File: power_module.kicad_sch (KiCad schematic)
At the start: 42 parts, among them IC1 LT8609AEDDM#PBF, IC2 LM2678SX-ADJ/NOPB, IC3 LM2678SX-ADJ/NOPB, IC4 LM2678SX-ADJ/NOPB, J1 Conn_01x02_Pin

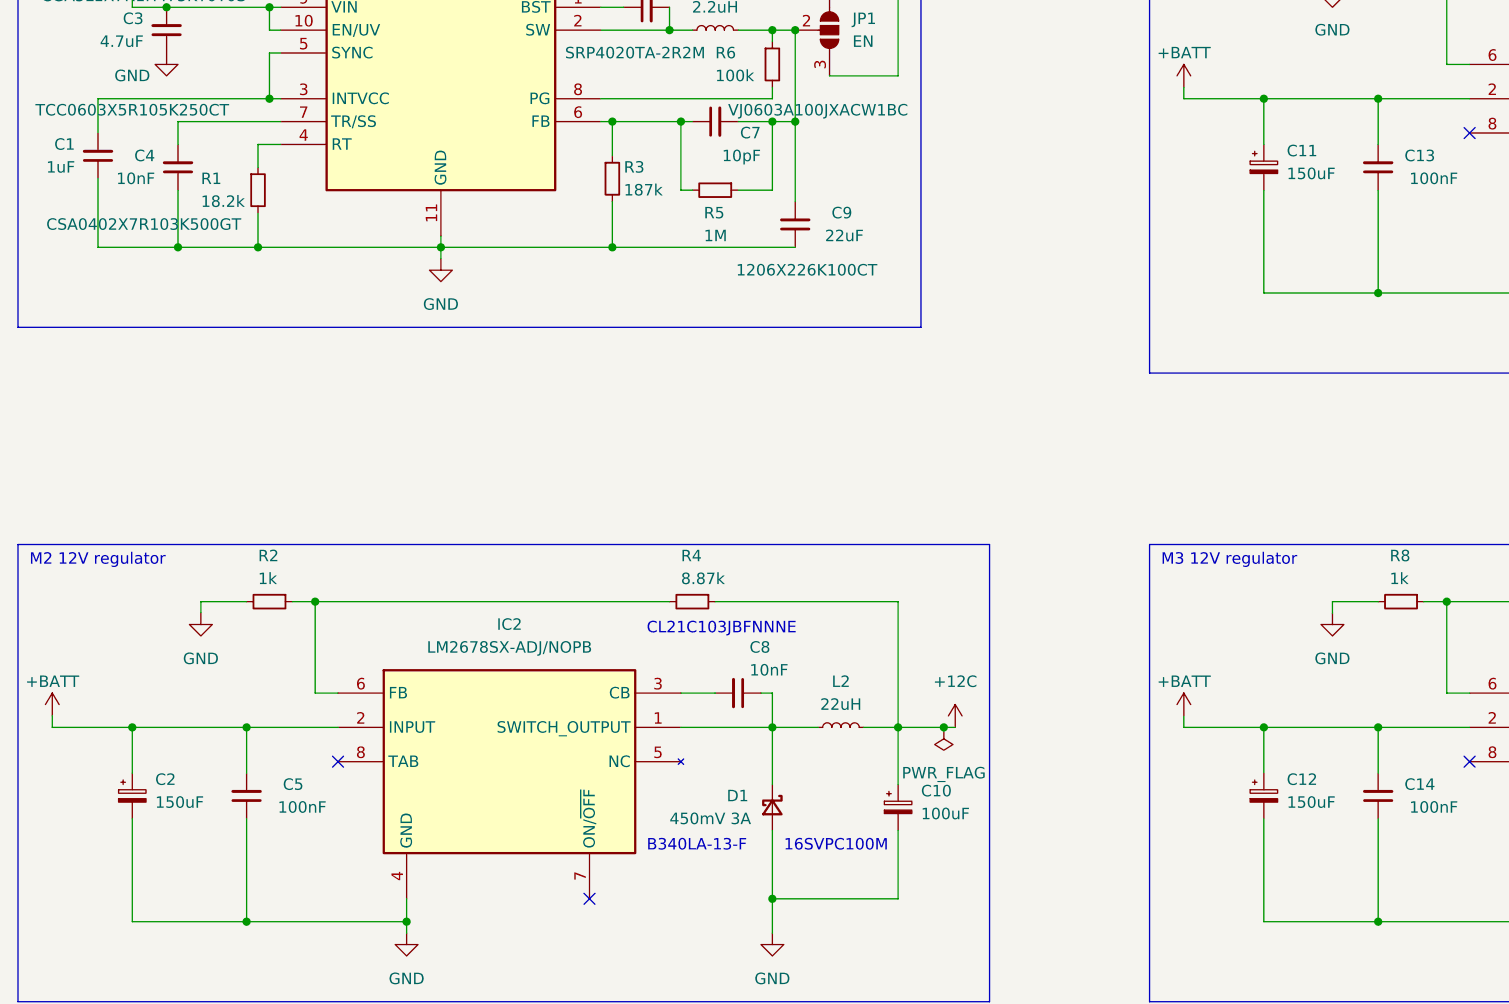
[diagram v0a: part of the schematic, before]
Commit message: completed 12 V regulators routing
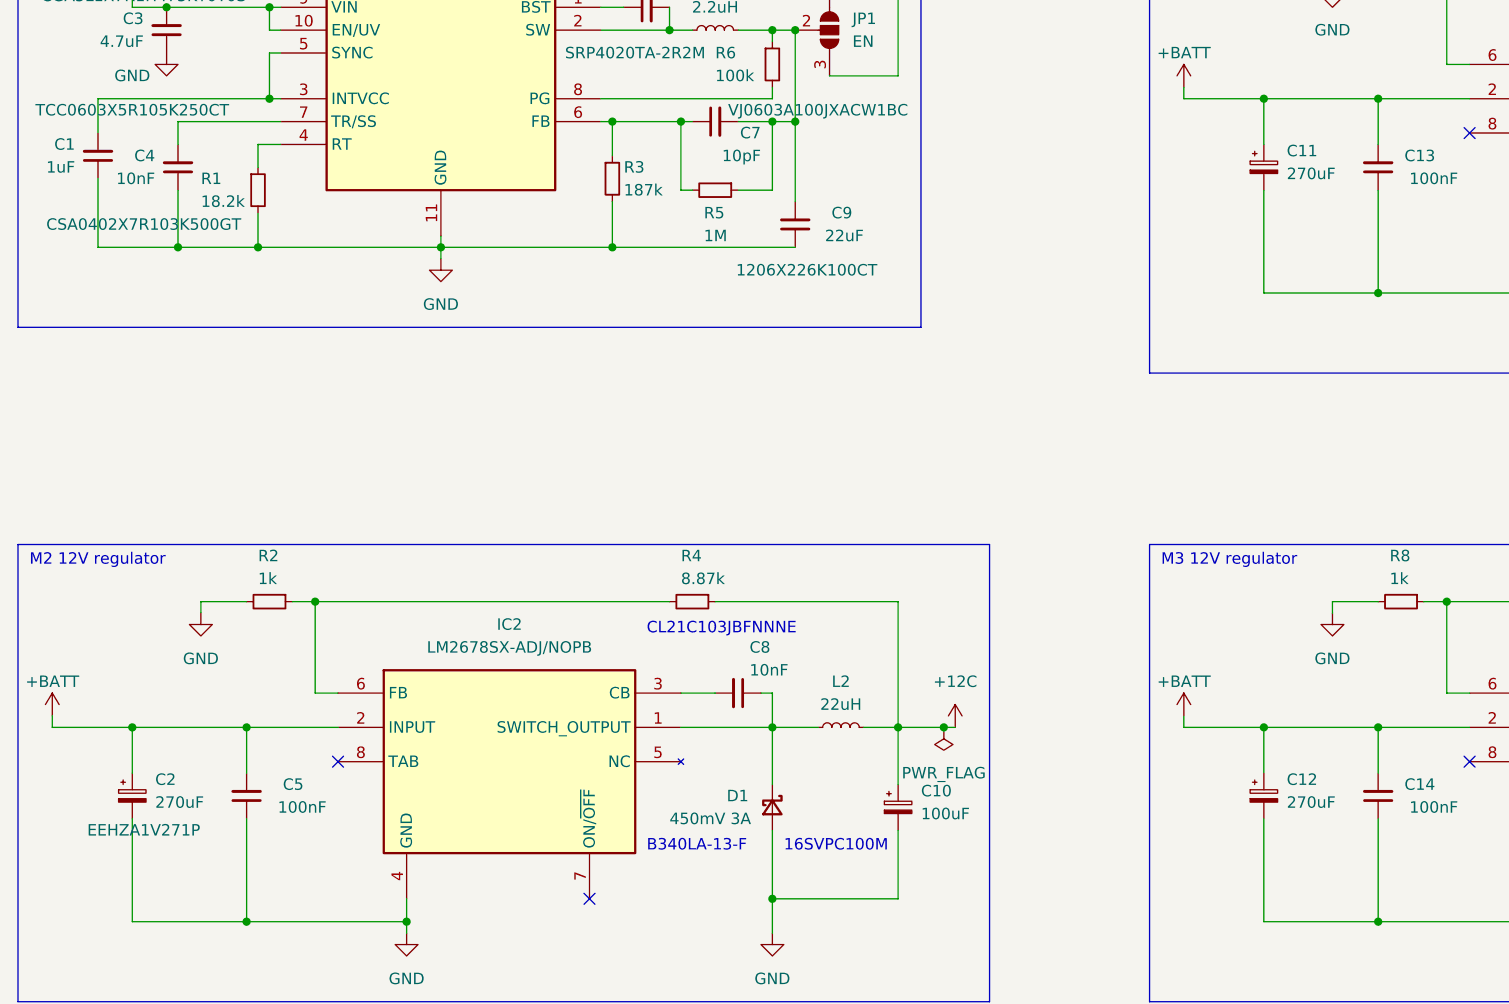
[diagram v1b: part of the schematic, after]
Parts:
- C11, C12: value 150uF -> 270uF; footprint SamacSys_Parts:EEHZT1E331UP -> SamacSys_Parts:EEHZS1H221P
- C2: value 150uF -> 270uF; footprint SamacSys_Parts:EEHZT1E331UP -> SamacSys_Parts:EEHZS1H221P; Part No. (none) -> EEHZA1V271P
- IC2, IC3, IC4: footprint SamacSys_Parts:KTW0007B -> rbc Custom Library:KTW0007B_custom
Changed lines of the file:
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@@
       (effects (font (size 1.27 1.27)))
     )
-    (property "Footprint" "SamacSys_Parts:KTW0007B" (at 217.17 202.87 0)
+    (property "Footprint" "rbc Custom Library:KTW0007B_custom" (at 217.17 202.87 0)
       (effects (font (size 1.27 1.27)) (justify left top) hide)
     )
@@
   )
   (symbol (lib_id "Device:C_Polarized_Small") (at 34.29 119.38 0) (unit 1)
-    (in_bom yes) (on_board yes) (dnp no) (fields_autoplaced)
+    (in_bom yes) (on_board yes) (dnp no)
     (property "Reference" "C2" (at 36.83 117.5639 0)
       (effects (font (size 1.27 1.27)) (justify left))
     )
-    (property "Value" "150uF" (at 36.83 120.1039 0)
-      (effects (font (size 1.27 1.27)) (justify left))
-    )
-    (property "Footprint" "SamacSys_Parts:EEHZT1E331UP" (at 34.29 119.38 0)
+    (property "Value" "270uF" (at 36.83 120.1039 0)
+      (effects (font (size 1.27 1.27)) (justify left))
+    )
+    (property "Footprint" "SamacSys_Parts:EEHZS1H221P" (at 34.29 119.38 0)
       (effects (font (size 1.27 1.27)) hide)
     )
     (property "Datasheet" "~" (at 34.29 119.38 0)
       (effects (font (size 1.27 1.27)) hide)
+    )
+    (property "Part No." "EEHZA1V271P" (at 35.56 123.19 0)
+      (effects (font (size 1.27 1.27)))
     )
     (pin "1")
@@
       (effects (font (size 1.27 1.27)))
     )
-    (property "Footprint" "SamacSys_Parts:KTW0007B" (at 91.44 202.87 0)
+    (property "Footprint" "rbc Custom Library:KTW0007B_custom" (at 91.44 202.87 0)
       (effects (font (size 1.27 1.27)) (justify left top) hide)
     )
@@
       (effects (font (size 1.27 1.27)) (justify left))
     )
-    (property "Value" "150uF" (at 162.56 120.1039 0)
-      (effects (font (size 1.27 1.27)) (justify left))
-    )
-    (property "Footprint" "SamacSys_Parts:EEHZT1E331UP" (at 160.02 119.38 0)
+    (property "Value" "270uF" (at 162.56 120.1039 0)
+      (effects (font (size 1.27 1.27)) (justify left))
+    )
+    (property "Footprint" "SamacSys_Parts:EEHZS1H221P" (at 160.02 119.38 0)
       (effects (font (size 1.27 1.27)) hide)
     )
@@
       (effects (font (size 1.27 1.27)) (justify left))
     )
-    (property "Value" "150uF" (at 162.56 50.2539 0)
-      (effects (font (size 1.27 1.27)) (justify left))
-    )
-    (property "Footprint" "SamacSys_Parts:EEHZT1E331UP" (at 160.02 49.53 0)
+    (property "Value" "270uF" (at 162.56 50.2539 0)
+      (effects (font (size 1.27 1.27)) (justify left))
+    )
+    (property "Footprint" "SamacSys_Parts:EEHZS1H221P" (at 160.02 49.53 0)
       (effects (font (size 1.27 1.27)) hide)
     )
     (property "Datasheet" "~" (at 160.02 49.53 0)
+      (effects (font (size 1.27 1.27)) hide)
+    )
+    (property "Part No." "" (at 160.02 49.53 0)
       (effects (font (size 1.27 1.27)) hide)
     )
@@
       (effects (font (size 1.27 1.27)))
     )
-    (property "Footprint" "SamacSys_Parts:KTW0007B" (at 217.17 133.02 0)
-      (effects (font (size 1.27 1.27)) (justify left top) hide)
-    )
+    (property "Footprint" "rbc Custom Library:KTW0007B_custom" (at 217.17 133.02 0)
+      (effects (font (size 1.27 1.27)) (justify left top) hide)
+    )

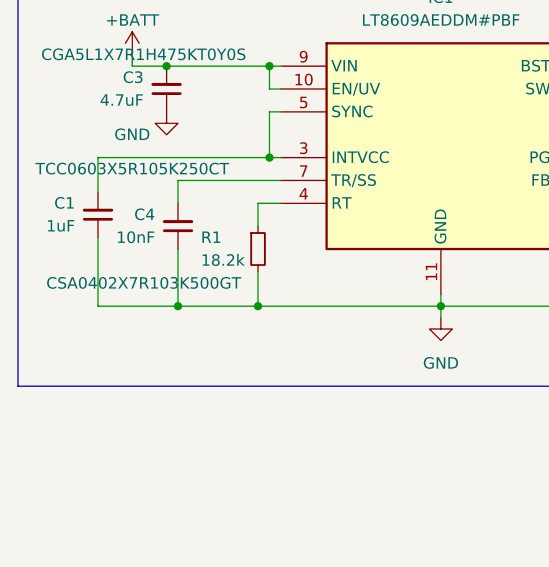
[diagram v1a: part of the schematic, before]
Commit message: fabrication ready
Note: some components' orientation may not be accurately described in PNP file, inspection required
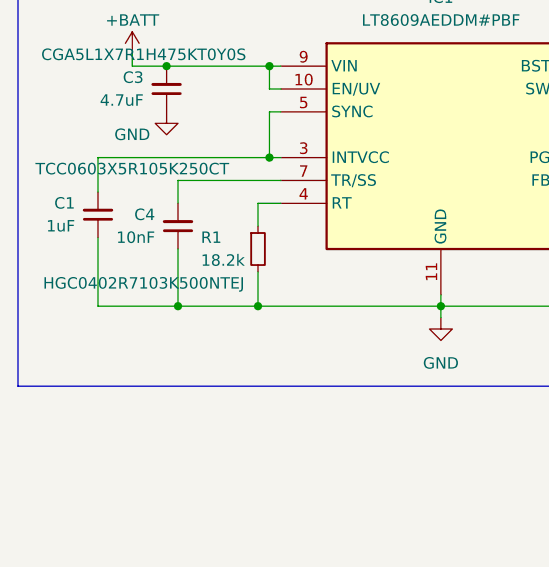
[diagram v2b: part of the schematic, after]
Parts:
- C4: Part No. CSA0402X7R103K500GT -> HGC0402R7103K500NTEJ
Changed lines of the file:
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@@
       (effects (font (size 1.27 1.27)) hide)
     )
-    (property "Part No." "CSA0402X7R103K500GT" (at 35.56 55.88 0)
+    (property "Part No." "HGC0402R7103K500NTEJ" (at 35.56 55.88 0)
       (effects (font (size 1.27 1.27)))
     )
